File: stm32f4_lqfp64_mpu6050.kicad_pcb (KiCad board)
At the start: 4 copper layers, 130 x 100 mm, 175 parts, among them M5 ALIS-CUSTOM-PARTS_POWERPADS, P1 CONN_01X08, P2 CONN_02X08, Q5 BSS138, Q6 CRYSTAL_50X32, U1 STM32F405R, U2 MPU6050, U3 LP2985LV, U4 LP2985LV, U5 W25Q80BV, U6 LMH1980, U7 TS5A3160, U8 TS5A3160, U9 LT6206, X1 CON-JST_SM04B-SRSS-TB, X2 CON-JST_SM04B-SRSS-TB, X4 CON-JST_SM04B-SRSS-TB

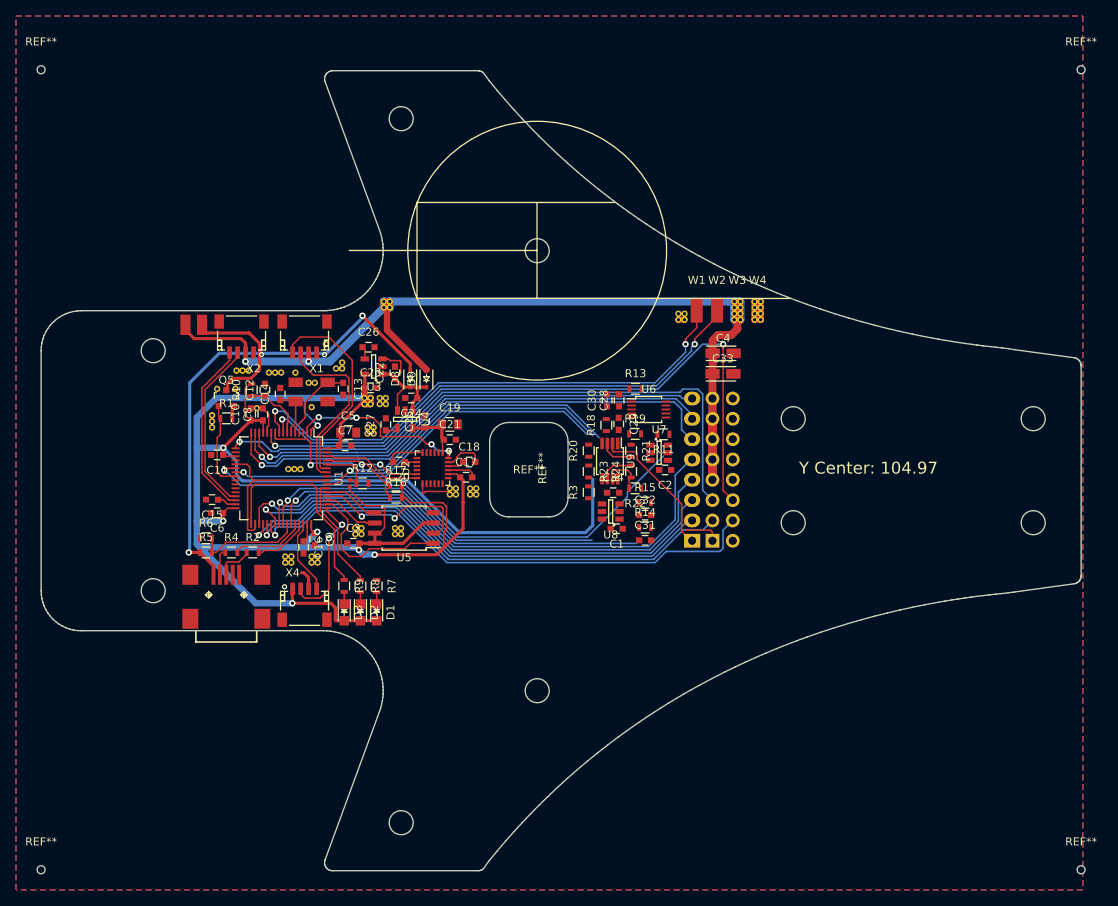
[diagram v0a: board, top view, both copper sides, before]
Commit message: routing finished - essential signals only
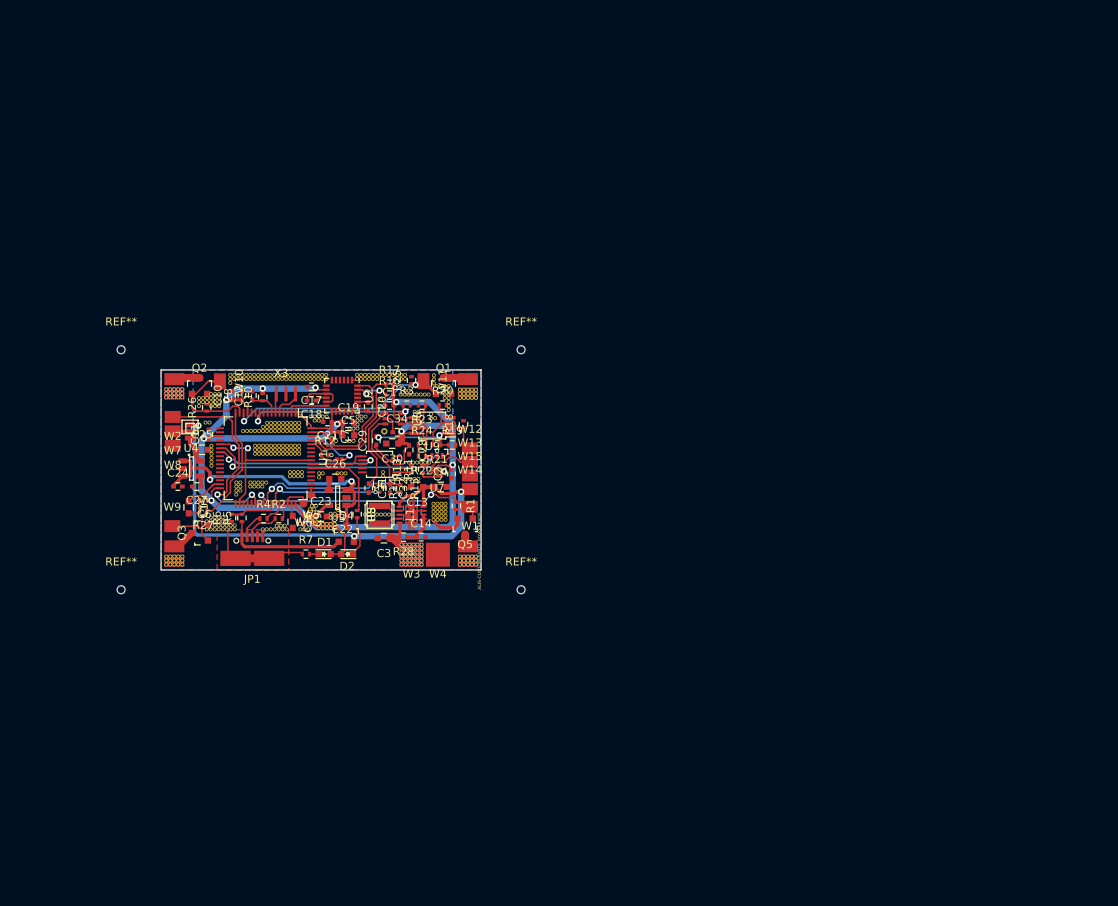
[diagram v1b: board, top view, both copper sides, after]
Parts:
- removed the ? at (173.1, 86.2)
- removed the ? at (172.3, 86.2)
- removed the ? at (126.7, 83.9)
- removed the ? at (126.0, 83.9)
- removed the ? at (126.0, 84.7)
- removed the ? at (126.7, 84.7)
- removed the ? at (170.6, 84.7)
- removed the ? at (170.6, 83.9)
- removed the ? at (169.8, 83.9)
- removed the ? at (169.8, 84.7)
- removed the ? at (170.6, 86.2)
- removed the ? at (120.0, 92.3)
- removed the ? at (170.6, 85.5)
- removed the ? at (169.8, 85.5)
- removed the ? at (169.8, 86.2)
- removed the ? at (124.3, 96.0)
- removed the ? at (124.3, 96.8)
- removed the ? at (123.6, 96.8)
- removed the ? at (104.5, 98.2)
- removed the ? at (104.5, 98.9)
- removed the ? at (104.5, 99.7)
- removed the ? at (123.2, 113.0)
- removed the ? at (172.3, 83.9)
- removed the ? at (122.4, 113.0)
- removed the ? at (122.4, 112.3)
- removed the ? at (123.2, 112.3)
- removed the ? at (117.7, 115.8)
- removed the ? at (117.7, 116.6)
- removed the ? at (117.0, 116.6)
- removed the ? at (117.0, 115.8)
- removed the ? at (127.4, 112.3)
- removed the ? at (128.1, 112.3)
- removed the ? at (128.1, 113.0)
- removed the ? at (117.0, 97.2)
- removed the ? at (127.4, 113.0)
- removed the ? at (123.6, 96.0)
- removed the ? at (136.8, 108.1)
- removed the ? at (137.5, 108.1)
- removed the ? at (137.5, 107.3)
- removed the ? at (136.8, 107.3)
- removed the ? at (134.2, 108.1)
- removed the ? at (134.2, 107.3)
- removed the ? at (135.0, 107.3)
- removed the ? at (135.0, 108.1)
- removed the ? at (173.1, 83.9)
- removed the ? at (124.7, 100.5)
- removed the ? at (125.5, 96.0)
- removed the ? at (126.2, 96.0)
- removed the ? at (126.2, 96.8)
- removed the ? at (125.5, 96.8)
- removed the ? at (124.0, 100.5)
- removed the ? at (124.0, 99.7)
- removed the ? at (124.7, 99.7)
- removed the ? at (162.8, 86.2)
- removed the ? at (163.6, 86.2)
- removed the ? at (173.1, 84.7)
- removed the ? at (162.8, 85.5)
- removed the ? at (163.6, 85.5)
- removed the ? at (110.1, 97.3)
- removed the ? at (115.6, 104.9)
- removed the ? at (114.8, 104.9)
- removed the ? at (114.0, 104.9)
- removed the ? at (114.4, 116.6)
- removed the ? at (113.7, 115.8)
- removed the ? at (113.7, 116.6)
- removed the ? at (114.4, 115.8)
- removed the ? at (172.3, 84.7)
- removed the ? at (120.8, 92.3)
- removed the ? at (120.8, 91.6)
- removed the ? at (118.7, 89.3)
- removed the ? at (117.3, 94.1)
- removed the ? at (116.6, 94.1)
- removed the ? at (114.9, 92.8)
- removed the ? at (113.2, 92.8)
- removed the ? at (112.4, 92.8)
- removed the ? at (111.6, 92.8)
- removed the ? at (109.1, 92.6)
- removed the ? at (173.1, 85.5)
- removed the ? at (108.3, 92.6)
- removed the ? at (107.6, 92.6)
- removed the ? at (105.2, 94.9)
- removed the ? at (107.4, 94.9)
- removed the ? at (172.3, 85.5)
- removed C33: 4u7, Capacitors_Tantalum_SMD:TantalC_SizeA_EIA-3216_Reflow
- removed D3: Red, LEDs:LED-0805
- removed D8, D9: D_Schottky_Small, Diodes_SMD:SOD-323
- removed P1: CONN_01X08, Pin_Headers:Pin_Header_Straight_1x08
- removed P2: CONN_02X08, Pin_Headers:Pin_Header_Straight_2x08
- removed Q6: CRYSTAL_50X32, minimal:CRYSTAL_50X32
- removed R9: 100R, Resistors_SMD:R_0603
- removed the REF** at (145.3, 104.8)
- removed the REF** at (144.1, 105.0)
- removed X1, X2, X4: CON-JST_SM04B-SRSS-TB, Connectors_JST_SH:Connectors_JST_SM04B-SRSS-TB
- added ?: , alis_parts:via_04_no_front_mask, F.Cu at (118.3, 93.6)
- added ?: , alis_parts:via_04_no_front_mask, F.Cu at (107.8, 93.6)
- added ?: , alis_parts:via_04_no_front_mask, F.Cu at (137.0, 116.3)
- added ?: , alis_parts:via_04_no_front_mask, F.Cu at (136.0, 116.3)
- added ?: , alis_parts:via_04_no_front_mask, F.Cu at (136.5, 116.3)
- added ?: , alis_parts:via_04_no_front_mask, F.Cu at (128.7, 114.8)
- added ?: , alis_parts:via_04_no_front_mask, F.Cu at (129.7, 114.8)
- added ?: , alis_parts:via_04_no_front_mask, F.Cu at (130.2, 114.8)
- added ?: , alis_parts:via_04_no_front_mask, F.Cu at (129.2, 114.8)
- added ?: , alis_parts:via_04_no_front_mask, F.Cu at (129.2, 116.3)
- added ?: , alis_parts:via_04_no_front_mask, F.Cu at (128.7, 116.3)
- added ?: , alis_parts:via_04_no_front_mask, F.Cu at (129.7, 116.3)
- added ?: , alis_parts:via_04_no_front_mask, F.Cu at (108.3, 93.6)
- added ?: , alis_parts:via_04_no_front_mask, F.Cu at (130.2, 116.3)
- added ?: , alis_parts:via_04_no_front_mask, F.Cu at (128.7, 115.8)
- added ?: , alis_parts:via_04_no_front_mask, F.Cu at (128.7, 115.3)
- added ?: , alis_parts:via_04_no_front_mask, F.Cu at (130.2, 115.3)
- added ?: , alis_parts:via_04_no_front_mask, F.Cu at (130.2, 115.8)
- added ?: , alis_parts:via_04_no_front_mask, F.Cu at (136.0, 95.5)
- added ?: , alis_parts:via_04_no_front_mask, F.Cu at (136.5, 95.5)
- added ?: , alis_parts:via_04_no_front_mask, F.Cu at (137.0, 95.5)
- added ?: , alis_parts:via_04_no_front_mask, F.Cu at (100.3, 95.4)
- added ?: , alis_parts:via_04_no_front_mask, F.Cu at (99.3, 95.4)
- added ?: , alis_parts:via_04_no_front_mask, F.Cu at (111.8, 93.6)
- added ?: , alis_parts:via_04_no_front_mask, F.Cu at (99.8, 95.4)
- added ?: , alis_parts:via_04_no_front_mask, F.Cu at (129.7, 115.3)
- added ?: , alis_parts:via_04_no_front_mask, F.Cu at (129.7, 114.3)
- added ?: , alis_parts:via_04_no_front_mask, F.Cu at (130.7, 114.8)
- added ?: , alis_parts:via_04_no_front_mask, F.Cu at (130.7, 114.3)
- added ?: , alis_parts:via_04_no_front_mask, F.Cu at (130.7, 115.3)
- added ?: , alis_parts:via_04_no_front_mask, F.Cu at (130.2, 114.3)
- added ?: , alis_parts:via_04_no_front_mask, F.Cu at (128.2, 114.8)
- added ?: , alis_parts:via_04_no_front_mask, F.Cu at (128.2, 115.3)
- added ?: , alis_parts:via_04_no_front_mask, F.Cu at (128.2, 114.3)
- added ?: , alis_parts:via_04_no_front_mask, F.Cu at (112.3, 93.6)
- added ?: , alis_parts:via_04_no_front_mask, F.Cu at (129.2, 114.3)
- added ?: , alis_parts:via_04_no_front_mask, F.Cu at (129.2, 115.3)
- added ?: , alis_parts:via_04_no_front_mask, F.Cu at (128.7, 114.3)
- added ?: , alis_parts:via_04_no_front_mask, F.Cu at (128.2, 116.3)
- added ?: , alis_parts:via_04_no_front_mask, F.Cu at (128.2, 116.8)
- added ?: , alis_parts:via_04_no_front_mask, F.Cu at (128.2, 115.8)
- added ?: , alis_parts:via_04_no_front_mask, F.Cu at (129.2, 115.8)
- added ?: , alis_parts:via_04_no_front_mask, F.Cu at (129.2, 116.8)
- added ?: , alis_parts:via_04_no_front_mask, F.Cu at (128.7, 116.8)
- added ?: , alis_parts:via_04_no_front_mask, F.Cu at (129.7, 116.8)
- added ?: , alis_parts:via_04_no_front_mask, F.Cu at (112.8, 93.6)
- added ?: , alis_parts:via_04_no_front_mask, F.Cu at (129.7, 115.8)
- added ?: , alis_parts:via_04_no_front_mask, F.Cu at (130.7, 116.3)
- added ?: , alis_parts:via_04_no_front_mask, F.Cu at (130.7, 115.8)
- added ?: , alis_parts:via_04_no_front_mask, F.Cu at (130.7, 116.8)
- added ?: , alis_parts:via_04_no_front_mask, F.Cu at (130.2, 116.8)
- added ?: , alis_parts:via_04_no_front_mask, F.Cu at (133.2, 109.2)
- added ?: , alis_parts:via_04_no_front_mask, F.Cu at (133.7, 109.2)
- added ?: , alis_parts:via_04_no_front_mask, F.Cu at (132.7, 109.2)
- added ?: , alis_parts:via_04_no_front_mask, F.Cu at (132.2, 109.2)
- added ?: , alis_parts:via_04_no_front_mask, F.Cu at (133.7, 110.2)
- added ?: , alis_parts:via_04_no_front_mask, F.Cu at (113.3, 93.6)
- added ?: , alis_parts:via_04_no_front_mask, F.Cu at (133.7, 111.2)
- added ?: , alis_parts:via_04_no_front_mask, F.Cu at (133.7, 109.7)
- added ?: , alis_parts:via_04_no_front_mask, F.Cu at (133.7, 110.7)
- added ?: , alis_parts:via_04_no_front_mask, F.Cu at (133.2, 109.7)
- added ?: , alis_parts:via_04_no_front_mask, F.Cu at (133.2, 110.7)
- added ?: , alis_parts:via_04_no_front_mask, F.Cu at (133.2, 110.2)
- added ?: , alis_parts:via_04_no_front_mask, F.Cu at (133.2, 111.2)
- added ?: , alis_parts:via_04_no_front_mask, F.Cu at (103.0, 109.2)
- added ?: , alis_parts:via_04_no_front_mask, F.Cu at (103.0, 109.7)
- added ?: , alis_parts:via_04_no_front_mask, F.Cu at (125.6, 96.2)
- added ?: , alis_parts:via_04_no_front_mask, F.Cu at (114.3, 93.6)
- added ?: , alis_parts:via_04_no_front_mask, F.Cu at (108.0, 107.6)
- added ?: , alis_parts:via_04_no_front_mask, F.Cu at (108.0, 107.1)
- added ?: , alis_parts:via_04_no_front_mask, F.Cu at (107.5, 108.1)
- added ?: , alis_parts:via_04_no_front_mask, F.Cu at (107.5, 107.6)
- added ?: , alis_parts:via_04_no_front_mask, F.Cu at (107.5, 107.1)
- added ?: , alis_parts:via_04_no_front_mask, F.Cu at (107.5, 106.6)
- added ?: , alis_parts:via_04_no_front_mask, F.Cu at (108.0, 106.6)
- added ?: , alis_parts:via_04_no_front_mask, F.Cu at (122.2, 101.4)
- added ?: , alis_parts:via_04_no_front_mask, F.Cu at (121.7, 101.4)
- added ?: , alis_parts:via_04_no_front_mask, F.Cu at (120.0, 101.4)
- added ?: , alis_parts:via_04_no_front_mask, F.Cu at (114.8, 93.6)
- added ?: , alis_parts:via_04_no_front_mask, F.Cu at (104.2, 99.1)
- added ?: , alis_parts:via_04_no_front_mask, F.Cu at (103.7, 99.1)
- added ?: , alis_parts:via_04_no_front_mask, F.Cu at (104.4, 104.5)
- added ?: , alis_parts:via_04_no_front_mask, F.Cu at (104.4, 104.0)
- added ?: , alis_parts:via_04_no_front_mask, F.Cu at (104.4, 103.5)
- added ?: , alis_parts:via_04_no_front_mask, F.Cu at (104.4, 103.0)
- added ?: , alis_parts:via_04_no_front_mask, F.Cu at (104.4, 102.5)
- added ?: , alis_parts:via_04_no_front_mask, F.Cu at (104.4, 102.0)
- added ?: , alis_parts:via_04_no_front_mask, F.Cu at (131.6, 104.1)
- added ?: , alis_parts:via_04_no_front_mask, F.Cu at (131.1, 104.1)
- added ?: , alis_parts:via_04_no_front_mask, F.Cu at (115.3, 93.6)
- added ?: , alis_parts:via_04_no_front_mask, F.Cu at (130.6, 104.1)
- added ?: , alis_parts:via_04_no_front_mask, F.Cu at (130.1, 104.1)
- added ?: , alis_parts:via_04_no_front_mask, F.Cu at (129.6, 104.1)
- added ?: , alis_parts:via_04_no_front_mask, F.Cu at (127.8, 106.1)
- added ?: , alis_parts:via_04_no_front_mask, F.Cu at (128.3, 106.1)
- added ?: , alis_parts:via_04_no_front_mask, F.Cu at (128.8, 106.1)
- added ?: , alis_parts:via_04_no_front_mask, F.Cu at (129.3, 106.1)
- added ?: , alis_parts:via_04_no_front_mask, F.Cu at (129.8, 106.1)
- added ?: , alis_parts:via_04_no_front_mask, F.Cu at (130.3, 106.1)
- added ?: , alis_parts:via_04_no_front_mask, F.Cu at (110.8, 107.1)
- added ?: , alis_parts:via_04_no_front_mask, F.Cu at (113.8, 93.6)
- added ?: , alis_parts:via_04_no_front_mask, F.Cu at (110.3, 107.1)
- added ?: , alis_parts:via_04_no_front_mask, F.Cu at (109.8, 107.1)
- added ?: , alis_parts:via_04_no_front_mask, F.Cu at (109.3, 107.1)
- added ?: , alis_parts:via_04_no_front_mask, F.Cu at (111.3, 106.6)
- added ?: , alis_parts:via_04_no_front_mask, F.Cu at (110.8, 106.6)
- added ?: , alis_parts:via_04_no_front_mask, F.Cu at (110.3, 106.6)
- added ?: , alis_parts:via_04_no_front_mask, F.Cu at (109.8, 106.6)
- added ?: , alis_parts:via_04_no_front_mask, F.Cu at (109.3, 106.6)
- added ?: , alis_parts:via_04_no_front_mask, F.Cu at (115.7, 105.8)
- added ?: , alis_parts:via_04_no_front_mask, F.Cu at (115.2, 105.8)
- added ?: , alis_parts:via_04_no_front_mask, F.Cu at (118.8, 93.6)
- added ?: , alis_parts:via_04_no_front_mask, F.Cu at (115.8, 93.6)
- added ?: , alis_parts:via_04_no_front_mask, F.Cu at (114.7, 105.8)
- added ?: , alis_parts:via_04_no_front_mask, F.Cu at (114.2, 105.8)
- added ?: , alis_parts:via_04_no_front_mask, F.Cu at (114.2, 105.3)
- added ?: , alis_parts:via_04_no_front_mask, F.Cu at (114.7, 105.3)
- added ?: , alis_parts:via_04_no_front_mask, F.Cu at (115.2, 105.3)
- added ?: , alis_parts:via_04_no_front_mask, F.Cu at (115.7, 105.3)
- added ?: , alis_parts:via_04_no_front_mask, F.Cu at (109.9, 102.0)
- added ?: , alis_parts:via_04_no_front_mask, F.Cu at (110.4, 102.0)
- added ?: , alis_parts:via_04_no_front_mask, F.Cu at (110.9, 102.0)
- added ?: , alis_parts:via_04_no_front_mask, F.Cu at (111.4, 102.0)
- added ?: , alis_parts:via_04_no_front_mask, F.Cu at (116.3, 93.6)
- added ?: , alis_parts:via_04_no_front_mask, F.Cu at (111.9, 102.0)
- added ?: , alis_parts:via_04_no_front_mask, F.Cu at (112.4, 102.0)
- added ?: , alis_parts:via_04_no_front_mask, F.Cu at (112.9, 102.0)
- added ?: , alis_parts:via_04_no_front_mask, F.Cu at (113.4, 102.0)
- added ?: , alis_parts:via_04_no_front_mask, F.Cu at (113.9, 102.0)
- added ?: , alis_parts:via_04_no_front_mask, F.Cu at (114.4, 102.0)
- added ?: , alis_parts:via_04_no_front_mask, F.Cu at (114.9, 102.0)
- added ?: , alis_parts:via_04_no_front_mask, F.Cu at (115.4, 102.0)
- added ?: , alis_parts:via_04_no_front_mask, F.Cu at (108.4, 100.1)
- added ?: , alis_parts:via_04_no_front_mask, F.Cu at (108.9, 100.1)
- added ?: , alis_parts:via_04_no_front_mask, F.Cu at (116.8, 93.6)
- added ?: , alis_parts:via_04_no_front_mask, F.Cu at (109.4, 100.1)
- added ?: , alis_parts:via_04_no_front_mask, F.Cu at (109.9, 100.1)
- added ?: , alis_parts:via_04_no_front_mask, F.Cu at (110.4, 100.1)
- added ?: , alis_parts:via_04_no_front_mask, F.Cu at (110.9, 100.1)
- added ?: , alis_parts:via_04_no_front_mask, F.Cu at (111.4, 100.1)
- added ?: , alis_parts:via_04_no_front_mask, F.Cu at (111.9, 100.1)
- added ?: , alis_parts:via_04_no_front_mask, F.Cu at (112.4, 100.1)
- added ?: , alis_parts:via_04_no_front_mask, F.Cu at (112.9, 100.1)
- added ?: , alis_parts:via_04_no_front_mask, F.Cu at (113.4, 100.1)
- added ?: , alis_parts:via_04_no_front_mask, F.Cu at (113.9, 100.1)
- added ?: , alis_parts:via_04_no_front_mask, F.Cu at (117.3, 93.6)
- added ?: , alis_parts:via_04_no_front_mask, F.Cu at (114.4, 100.1)
- added ?: , alis_parts:via_04_no_front_mask, F.Cu at (114.9, 100.1)
- added ?: , alis_parts:via_04_no_front_mask, F.Cu at (115.4, 100.1)
- added ?: , alis_parts:via_04_no_front_mask, F.Cu at (117.8, 98.8)
- added ?: , alis_parts:via_04_no_front_mask, F.Cu at (117.3, 98.8)
- added ?: , alis_parts:via_04_no_front_mask, F.Cu at (116.8, 98.3)
- added ?: , alis_parts:via_04_no_front_mask, F.Cu at (117.3, 98.3)
- added ?: , alis_parts:via_04_no_front_mask, F.Cu at (117.8, 98.3)
- added ?: , alis_parts:via_04_no_front_mask, F.Cu at (118.3, 98.3)
- added ?: , alis_parts:via_04_no_front_mask, F.Cu at (118.8, 98.3)
- added ?: , alis_parts:via_04_no_front_mask, F.Cu at (117.8, 93.6)
- added ?: , alis_parts:via_04_no_front_mask, F.Cu at (121.7, 99.8)
- added ?: , alis_parts:via_04_no_front_mask, F.Cu at (122.2, 99.8)
- added ?: , alis_parts:via_04_no_front_mask, F.Cu at (122.7, 99.8)
- added ?: , alis_parts:via_04_no_front_mask, F.Cu at (122.7, 99.3)
- added ?: , alis_parts:via_04_no_front_mask, F.Cu at (122.7, 98.8)
- added ?: , alis_parts:via_04_no_front_mask, F.Cu at (122.7, 98.3)
- added ?: , alis_parts:via_04_no_front_mask, F.Cu at (123.2, 98.8)
- added ?: , alis_parts:via_04_no_front_mask, F.Cu at (123.2, 98.3)
- added ?: , alis_parts:via_04_no_front_mask, F.Cu at (123.7, 98.3)
- added ?: , alis_parts:via_04_no_front_mask, F.Cu at (129.8, 97.7)
- added ?: , alis_parts:via_04_no_front_mask, F.Cu at (128.1, 93.6)
- added ?: , alis_parts:via_04_no_front_mask, F.Cu at (130.3, 97.7)
- added ?: , alis_parts:via_04_no_front_mask, F.Cu at (131.9, 98.0)
- added ?: , alis_parts:via_04_no_front_mask, F.Cu at (131.9, 98.5)
- added ?: , alis_parts:via_04_no_front_mask, F.Cu at (132.4, 98.5)
- added ?: , alis_parts:via_04_no_front_mask, F.Cu at (129.1, 104.1)
- added ?: , alis_parts:via_04_no_front_mask, F.Cu at (125.9, 105.8)
- added ?: , alis_parts:via_04_no_front_mask, F.Cu at (125.9, 105.3)
- added ?: , alis_parts:via_04_no_front_mask, F.Cu at (132.2, 109.7)
- added ?: , alis_parts:via_04_no_front_mask, F.Cu at (132.7, 109.7)
- added ?: , alis_parts:via_04_no_front_mask, F.Cu at (132.7, 110.2)
- added ?: , alis_parts:via_04_no_front_mask, F.Cu at (128.6, 93.6)
- added ?: , alis_parts:via_04_no_front_mask, F.Cu at (132.2, 110.2)
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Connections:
- net BUZZER renamed M4
- net Net-(C29-Pad2) renamed video_buffered
- net Net-(C31-Pad1) renamed W_Filtered
- net Net-(C32-Pad1) renamed B_Filtered
- net Net-(JP2-Pad2) renamed BOOT0
- net Net-(R22-Pad2) renamed bw_buffered
- C13 pad 1: Net-(C13-Pad1) -> 5V
- C19 pad 1: 3.3V_SEN -> 3.3V
- C21 pad 1: 3.3V_SEN -> 3.3V
- C25 pad 1: 3.3V_SEN -> 3.3V_EXT
- C28 pad 1: Net-(C28-Pad1) -> 3.3V
- C3 pad 1: GND -> VBAT
- C3 pad 2: 3.3V -> GND
- C30 pad 1: Net-(C30-Pad1) -> 3.3V
- C4 pad 1: VBAT -> 5V
- Q5 pad 1: MCU_BUZZER -> TIM8_CH4
- R1 pad 1: MCU_BUZZER -> TIM8_CH4
- U1 pad 5: Net-(C13-Pad1) -> Net-(U1-Pad5)
- U1 pad 6: Net-(C14-Pad1) -> Net-(U1-Pad6)
- U2 pad 13: 3.3V_SEN -> 3.3V
- U4 pad 5: 3.3V_SEN -> 3.3V_EXT
- U5 pad 1: FLASH_CS -> 5V
- U5 pad 2: MISO -> Net-(L1-Pad1)
- U5 pad 3: 3.3V -> GND
- U5 pad 4: GND -> Net-(L1-Pad2)
- U5 pad 5: MOSI -> VBAT
- U5 pad 6: SCK -> Net-(C14-Pad1)
- U5 pad 7: 3.3V -> Net-(C14-Pad1)
- U5 pad 8: 3.3V -> Net-(C14-Pad1)
- U6 pad 3: Net-(C30-Pad1) -> 3.3V
- W1 pad 1: ADC2 -> TIM8_CH4
- W2 pad 1: ADC1 -> TIM8_CH2/FRSKY_RSSI/DSM
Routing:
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- added copper zone on B.Cu, net VBAT
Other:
- board size 130 x 100 mm -> 40 x 25 mm
- board text removed: "Alexander Tuxen 2016"
- board text removed: "Flexi Main"
- board text removed: "PPM Servo Back Left Right"
- board text removed: "Vin Vout GND PWM7 PWM8 DSM PWM5 PWM6 ADC3"
- board text removed: "Y Center: 104.97"

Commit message: minor changes
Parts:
- removed the ? at (118.3, 93.6)
- removed the ? at (107.8, 93.6)
- removed the ? at (137.0, 116.3)
- removed the ? at (136.0, 116.3)
- removed the ? at (136.5, 116.3)
- removed the ? at (128.7, 114.8)
- removed the ? at (129.7, 114.8)
- removed the ? at (130.2, 114.8)
- removed the ? at (129.2, 114.8)
- removed the ? at (129.2, 116.3)
- removed the ? at (128.7, 116.3)
- removed the ? at (129.7, 116.3)
- removed the ? at (108.3, 93.6)
- removed the ? at (130.2, 116.3)
- removed the ? at (128.7, 115.8)
- removed the ? at (128.7, 115.3)
- removed the ? at (130.2, 115.3)
- removed the ? at (130.2, 115.8)
- removed the ? at (136.0, 95.5)
- removed the ? at (136.5, 95.5)
- removed the ? at (137.0, 95.5)
- removed the ? at (100.3, 95.4)
- removed the ? at (99.3, 95.4)
- removed the ? at (111.8, 93.6)
- removed the ? at (99.8, 95.4)
- removed the ? at (129.7, 115.3)
- removed the ? at (129.7, 114.3)
- removed the ? at (130.7, 114.8)
- removed the ? at (130.7, 114.3)
- removed the ? at (130.7, 115.3)
- removed the ? at (130.2, 114.3)
- removed the ? at (128.2, 114.8)
- removed the ? at (128.2, 115.3)
- removed the ? at (128.2, 114.3)
- removed the ? at (112.3, 93.6)
- removed the ? at (129.2, 114.3)
- removed the ? at (129.2, 115.3)
- removed the ? at (128.7, 114.3)
- removed the ? at (128.2, 116.3)
- removed the ? at (128.2, 116.8)
- removed the ? at (128.2, 115.8)
- removed the ? at (129.2, 115.8)
- removed the ? at (129.2, 116.8)
- removed the ? at (128.7, 116.8)
- removed the ? at (129.7, 116.8)
- removed the ? at (112.8, 93.6)
- removed the ? at (129.7, 115.8)
- removed the ? at (130.7, 116.3)
- removed the ? at (130.7, 115.8)
- removed the ? at (130.7, 116.8)
- removed the ? at (130.2, 116.8)
- removed the ? at (133.2, 109.2)
- removed the ? at (133.7, 109.2)
- removed the ? at (132.7, 109.2)
- removed the ? at (132.2, 109.2)
- removed the ? at (133.7, 110.2)
- removed the ? at (113.3, 93.6)
- removed the ? at (133.7, 111.2)
- removed the ? at (133.7, 109.7)
- removed the ? at (133.7, 110.7)
- removed the ? at (133.2, 109.7)
- removed the ? at (133.2, 110.7)
- removed the ? at (133.2, 110.2)
- removed the ? at (133.2, 111.2)
- removed the ? at (103.0, 109.2)
- removed the ? at (103.0, 109.7)
- removed the ? at (125.6, 96.2)
- removed the ? at (114.3, 93.6)
- removed the ? at (108.0, 107.6)
- removed the ? at (108.0, 107.1)
- removed the ? at (107.5, 108.1)
- removed the ? at (107.5, 107.6)
- removed the ? at (107.5, 106.6)
- removed the ? at (108.0, 106.6)
- removed the ? at (122.2, 101.4)
- removed the ? at (121.7, 101.4)
- removed the ? at (120.0, 101.4)
- removed the ? at (114.8, 93.6)
- removed the ? at (104.2, 99.1)
- removed the ? at (103.7, 99.1)
- removed the ? at (104.4, 104.5)
- removed the ? at (104.4, 104.0)
- removed the ? at (104.4, 103.5)
- removed the ? at (104.4, 103.0)
- removed the ? at (104.4, 102.5)
- removed the ? at (104.4, 102.0)
- removed the ? at (131.6, 104.1)
- removed the ? at (131.1, 104.1)
- removed the ? at (115.3, 93.6)
- removed the ? at (130.6, 104.1)
- removed the ? at (130.1, 104.1)
- removed the ? at (129.6, 104.1)
- removed the ? at (127.8, 106.1)
- removed the ? at (128.3, 106.1)
- removed the ? at (128.8, 106.1)
- removed the ? at (129.3, 106.1)
- removed the ? at (129.8, 106.1)
- removed the ? at (130.3, 106.1)
- removed the ? at (110.8, 107.1)
- removed the ? at (113.8, 93.6)
- removed the ? at (110.3, 107.1)
- removed the ? at (109.8, 107.1)
- removed the ? at (109.3, 107.1)
- removed the ? at (111.3, 106.6)
- removed the ? at (110.8, 106.6)
- removed the ? at (110.3, 106.6)
- removed the ? at (109.8, 106.6)
- removed the ? at (109.3, 106.6)
- removed the ? at (115.7, 105.8)
- removed the ? at (115.2, 105.8)
- removed the ? at (118.8, 93.6)
- removed the ? at (115.8, 93.6)
- removed the ? at (114.7, 105.8)
- removed the ? at (114.2, 105.8)
- removed the ? at (114.2, 105.3)
- removed the ? at (114.7, 105.3)
- removed the ? at (115.2, 105.3)
- removed the ? at (115.7, 105.3)
- removed the ? at (109.9, 102.0)
- removed the ? at (110.4, 102.0)
- removed the ? at (110.9, 102.0)
- removed the ? at (111.4, 102.0)
- removed the ? at (116.3, 93.6)
- removed the ? at (111.9, 102.0)
- removed the ? at (112.4, 102.0)
- removed the ? at (112.9, 102.0)
- removed the ? at (113.4, 102.0)
- removed the ? at (113.9, 102.0)
- removed the ? at (114.4, 102.0)
- removed the ? at (114.9, 102.0)
- removed the ? at (115.4, 102.0)
- removed the ? at (108.4, 100.1)
- removed the ? at (108.9, 100.1)
- removed the ? at (116.8, 93.6)
- removed the ? at (109.4, 100.1)
- removed the ? at (109.9, 100.1)
- removed the ? at (110.4, 100.1)
- removed the ? at (110.9, 100.1)
- removed the ? at (111.4, 100.1)
- removed the ? at (111.9, 100.1)
- removed the ? at (112.4, 100.1)
- removed the ? at (112.9, 100.1)
- removed the ? at (113.4, 100.1)
- removed the ? at (113.9, 100.1)
- removed the ? at (117.3, 93.6)
- removed the ? at (114.4, 100.1)
- removed the ? at (114.9, 100.1)
- removed the ? at (115.4, 100.1)
- removed the ? at (117.8, 98.8)
- removed the ? at (117.3, 98.8)
- removed the ? at (116.8, 98.3)
- removed the ? at (117.3, 98.3)
- removed the ? at (117.8, 98.3)
- removed the ? at (118.3, 98.3)
- removed the ? at (118.8, 98.3)
- removed the ? at (117.8, 93.6)
- removed the ? at (121.7, 99.8)
- removed the ? at (122.2, 99.8)
- removed the ? at (122.7, 99.8)
- removed the ? at (122.7, 99.3)
- removed the ? at (122.7, 98.8)
- removed the ? at (122.7, 98.3)
- removed the ? at (123.2, 98.8)
- removed the ? at (123.7, 98.3)
- removed the ? at (129.8, 97.7)
- removed the ? at (128.1, 93.6)
- removed the ? at (130.3, 97.7)
- removed the ? at (131.9, 98.0)
- removed the ? at (131.9, 98.5)
- removed the ? at (132.4, 98.5)
- removed the ? at (129.1, 104.1)
- removed the ? at (125.9, 105.8)
- removed the ? at (125.9, 105.3)
- removed the ? at (132.2, 109.7)
- removed the ? at (132.7, 109.7)
- removed the ? at (132.7, 110.2)
- removed the ? at (128.6, 93.6)
- removed the ? at (132.2, 110.2)
- removed the ? at (132.2, 110.7)
- removed the ? at (132.7, 110.7)
- removed the ? at (132.2, 111.2)
- removed the ? at (132.7, 111.2)
- removed the ? at (99.8, 94.9)
- removed the ? at (100.3, 94.9)
- removed the ? at (100.8, 94.9)
- removed the ? at (99.8, 95.9)
- removed the ? at (100.3, 95.9)
- removed the ? at (124.6, 93.6)
- removed the ? at (100.8, 95.9)
- removed the ? at (100.8, 95.4)
- removed the ? at (98.8, 95.9)
- removed the ? at (98.8, 95.4)
- removed the ? at (98.8, 94.9)
- removed the ? at (99.3, 94.9)
- removed the ? at (99.3, 95.9)
- removed the ? at (99.8, 115.8)
- removed the ? at (100.3, 115.8)
- removed the ? at (100.8, 115.8)
- removed the ? at (124.1, 93.6)
- removed the ? at (99.8, 116.8)
- removed the ? at (100.3, 116.8)
- removed the ? at (100.8, 116.8)
- removed the ? at (100.8, 116.3)
- removed the ? at (98.8, 116.8)
- removed the ? at (98.8, 116.3)
- removed the ? at (98.8, 115.8)
- removed the ? at (99.3, 115.8)
- removed the ? at (99.3, 116.8)
- removed the ? at (136.5, 115.8)
- removed the ? at (123.6, 93.6)
- removed the ? at (137.0, 115.8)
- removed the ? at (137.5, 115.8)
- removed the ? at (136.5, 116.8)
- removed the ? at (137.0, 116.8)
- removed the ? at (137.5, 116.8)
- removed the ? at (137.5, 116.3)
- removed the ? at (135.5, 116.8)
- removed the ? at (135.5, 116.3)
- removed the ? at (135.5, 115.8)
- removed the ? at (136.0, 115.8)
- removed the ? at (109.8, 93.6)
- removed the ? at (125.1, 93.6)
- removed the ? at (136.0, 116.8)
- removed the ? at (135.5, 96.0)
- removed the ? at (135.5, 95.5)
- removed the ? at (135.5, 95.0)
- removed the ? at (136.0, 95.0)
- removed the ? at (136.0, 96.0)
- removed the ? at (136.5, 96.0)
- removed the ? at (136.5, 95.0)
- removed the ? at (137.0, 95.0)
- removed the ? at (137.0, 96.0)
- removed the ? at (123.1, 93.6)
- removed the ? at (137.5, 96.0)
- removed the ? at (137.5, 95.5)
- removed the ? at (137.5, 95.0)
- removed the ? at (118.8, 93.1)
- removed the ? at (118.3, 93.1)
- removed the ? at (117.8, 93.1)
- removed the ? at (117.3, 93.1)
- removed the ? at (116.8, 93.1)
- removed the ? at (116.3, 93.1)
- removed the ? at (115.8, 93.1)
- removed the ? at (122.6, 93.6)
- removed the ? at (115.3, 93.1)
- removed the ? at (114.8, 93.1)
- removed the ? at (114.3, 93.1)
- removed the ? at (113.8, 93.1)
- removed the ? at (113.3, 93.1)
- removed the ? at (112.8, 93.1)
- removed the ? at (112.3, 93.1)
- removed the ? at (111.8, 93.1)
- removed the ? at (111.3, 93.1)
- removed the ? at (110.8, 93.1)
- removed the ? at (120.2, 109.5)
- removed the ? at (110.3, 93.1)
- removed the ? at (109.8, 93.1)
- removed the ? at (122.6, 93.1)
- removed the ? at (123.1, 93.1)
- removed the ? at (123.6, 93.1)
- removed the ? at (124.1, 93.1)
- removed the ? at (124.6, 93.1)
- removed the ? at (125.1, 93.1)
- removed the ? at (125.6, 93.1)
- removed the ? at (126.1, 93.1)
- removed the ? at (120.2, 110.0)
- removed the ? at (126.6, 93.1)
- removed the ? at (127.1, 93.1)
- removed the ? at (127.6, 93.1)
- removed the ? at (128.1, 93.1)
- removed the ? at (128.6, 93.1)
- removed the ? at (129.1, 95.1)
- removed the ? at (128.6, 95.1)
- removed the ? at (128.1, 95.6)
- removed the ? at (128.6, 95.6)
- removed the ? at (129.1, 95.6)
- removed the ? at (119.3, 110.5)
- removed the ? at (129.6, 95.6)
- removed the ? at (130.1, 95.6)
- removed the ? at (130.6, 95.6)
- removed the ? at (131.1, 95.6)
- removed the ? at (131.6, 95.6)
- removed the ? at (134.1, 97.5)
- removed the ? at (134.1, 97.0)
- removed the ? at (134.1, 96.5)
- removed the ? at (132.2, 93.2)
- removed the ? at (132.2, 93.7)
- removed the ? at (119.8, 110.5)
- removed the ? at (132.2, 94.2)
- removed the ? at (132.6, 94.5)
- removed the ? at (133.1, 94.5)
- removed the ? at (133.6, 94.5)
- removed the ? at (133.6, 95.0)
- removed the ? at (133.6, 95.5)
- removed the ? at (133.6, 96.0)
- removed the ? at (134.1, 96.0)
- removed the ? at (134.1, 95.5)
- removed the ? at (134.1, 95.0)
- removed the ? at (119.8, 111.0)
- removed the ? at (134.1, 94.5)
- removed the ? at (109.3, 93.1)
- removed the ? at (108.8, 93.1)
- removed the ? at (108.3, 93.1)
- removed the ? at (107.8, 93.1)
- removed the ? at (107.3, 93.1)
- removed the ? at (106.8, 94.1)
- removed the ? at (106.8, 93.6)
- removed the ? at (106.8, 93.1)
- removed the ? at (102.9, 97.0)
- removed the ? at (119.3, 111.0)
- removed the ? at (102.9, 96.5)
- removed the ? at (102.9, 96.0)
- removed the ? at (103.4, 96.0)
- removed the ? at (103.4, 96.5)
- removed the ? at (103.9, 96.5)
- removed the ? at (103.9, 96.0)
- removed the ? at (104.4, 96.0)
- removed the ? at (104.4, 95.5)
- removed the ? at (104.9, 96.0)
- removed the ? at (104.9, 95.5)
- removed the ? at (116.3, 110.8)
- removed the ? at (105.4, 96.0)
- removed the ? at (105.4, 96.5)
- removed the ? at (104.9, 96.5)
- removed the ? at (104.4, 96.5)
- removed the ? at (104.4, 97.0)
- removed the ? at (104.9, 97.0)
- removed the ? at (105.4, 97.0)
- removed the ? at (105.8, 110.9)
- removed the ? at (105.3, 110.9)
- removed the ? at (110.3, 93.6)
- removed the ? at (116.8, 110.8)
- removed the ? at (104.8, 110.9)
- removed the ? at (104.3, 110.9)
- removed the ? at (106.3, 111.4)
- removed the ? at (105.8, 111.4)
- removed the ? at (105.3, 111.4)
- removed the ? at (104.8, 111.4)
- removed the ? at (104.3, 111.4)
- removed the ? at (103.8, 111.4)
- removed the ? at (104.8, 111.9)
- removed the ? at (105.3, 111.9)
- removed the ? at (116.8, 111.3)
- removed the ? at (105.8, 111.9)
- removed the ? at (106.3, 111.9)
- removed the ? at (106.8, 111.9)
- removed the ? at (107.3, 111.9)
- removed the ? at (107.3, 112.4)
- removed the ? at (106.8, 112.4)
- removed the ? at (106.3, 112.4)
- removed the ? at (105.8, 112.4)
- removed the ? at (105.3, 112.4)
- removed the ? at (104.8, 112.4)
- removed the ? at (117.3, 111.3)
- removed the ? at (104.3, 112.4)
- removed the ? at (103.8, 112.4)
- removed the ? at (113.6, 112.0)
- removed the ? at (113.1, 112.0)
- removed the ? at (112.6, 112.0)
- removed the ? at (110.8, 112.4)
- removed the ? at (111.3, 112.4)
- removed the ? at (111.8, 112.4)
- removed the ? at (112.3, 112.4)
- removed the ? at (112.8, 112.4)
- removed the ? at (117.3, 111.8)
- removed the ? at (113.3, 112.4)
- removed the ? at (113.8, 112.4)
- removed the ? at (115.5, 111.7)
- removed the ? at (115.5, 112.4)
- removed the ? at (116.0, 112.4)
- removed the ? at (116.5, 112.4)
- removed the ? at (123.6, 110.6)
- removed the ? at (124.1, 110.6)
- removed the ? at (124.6, 110.6)
- removed the ? at (125.1, 110.6)
- removed the ? at (119.8, 111.8)
- removed the ? at (125.6, 110.6)
- removed the ? at (126.1, 110.6)
- removed the ? at (126.6, 110.6)
- removed the ? at (117.5, 109.5)
- removed the ? at (117.0, 109.5)
- removed the ? at (116.7, 109.9)
- removed the ? at (117.2, 109.9)
- removed the ? at (117.9, 105.9)
- removed the ? at (118.3, 105.4)
- removed the ? at (117.9, 105.4)
- removed the ? at (119.3, 111.8)
- removed the ? at (120.2, 105.4)
- removed the ? at (120.7, 105.4)
- removed the ? at (121.2, 105.4)
- removed the ? at (126.0, 100.2)
- removed the ? at (118.8, 111.8)
- removed the ? at (118.3, 111.8)
- removed the ? at (117.8, 111.8)
- removed the ? at (117.8, 112.3)
- removed the ? at (109.3, 93.6)
- removed the ? at (118.3, 112.3)
- removed the ? at (118.8, 112.3)
- removed the ? at (119.3, 112.3)
- removed the ? at (119.8, 112.3)
- removed the ? at (111.9, 99.1)
- removed the ? at (111.4, 99.1)
- removed the ? at (112.4, 99.1)
- removed the ? at (112.9, 99.1)
- removed the ? at (113.9, 99.1)
- removed the ? at (115.4, 99.1)
- removed the ? at (110.8, 93.6)
- removed the ? at (114.9, 99.1)
- removed the ? at (114.4, 99.1)
- removed the ? at (113.4, 99.1)
- removed the ? at (110.9, 99.6)
- removed the ? at (112.4, 99.6)
- removed the ? at (111.9, 99.6)
- removed the ? at (112.9, 99.6)
- removed the ? at (111.4, 99.6)
- removed the ? at (113.4, 99.6)
- removed the ? at (114.4, 99.6)
- removed the ? at (111.3, 93.6)
- removed the ? at (115.4, 99.6)
- removed the ? at (114.9, 99.6)
- removed the ? at (113.9, 99.6)
- removed the ? at (109.9, 103.0)
- removed the ? at (110.4, 103.0)
- removed the ? at (110.9, 103.0)
- removed the ? at (112.4, 103.0)
- removed the ? at (111.9, 103.0)
- removed the ? at (112.9, 103.0)
- removed the ? at (111.4, 103.0)
- removed the ? at (108.8, 93.6)
- removed the ? at (113.4, 103.0)
- removed the ? at (114.4, 103.0)
- removed the ? at (115.4, 103.0)
- removed the ? at (114.9, 103.0)
- removed the ? at (113.9, 103.0)
- removed the ? at (109.9, 102.5)
- removed the ? at (110.4, 102.5)
- removed the ? at (110.9, 102.5)
- removed the ? at (112.4, 102.5)
- removed the ? at (111.9, 102.5)
- removed the ? at (107.3, 93.6)
- removed the ? at (112.9, 102.5)
- removed the ? at (111.4, 102.5)
- removed the ? at (113.4, 102.5)
- removed the ? at (114.4, 102.5)
- removed the ? at (115.4, 102.5)
- removed the ? at (114.9, 102.5)
- removed the ? at (113.9, 102.5)
- removed the ? at (99.8, 116.3)
- removed the ? at (100.3, 116.3)
- removed the ? at (99.3, 116.3)
- removed REF** (x4): PositioningHole_1mm, alis_parts:PositioningHole_1mm
- added ?: , alis_parts:via_04_no_front_mask, F.Cu at (117.6, 99.1)
- added ?: , alis_parts:via_04_no_front_mask, F.Cu at (112.5, 113.0)
- added ?: , alis_parts:via_04_no_front_mask, F.Cu at (127.1, 99.1)
- added ?: , alis_parts:via_04_no_front_mask, F.Cu at (126.2, 100.3)
- added ?: , alis_parts:via_04_no_front_mask, F.Cu at (126.4, 102.6)
- added ?: , alis_parts:via_04_no_front_mask, F.Cu at (127.1, 102.6)
- added ?: , alis_parts:via_04_no_front_mask, F.Cu at (127.9, 102.6)
- added ?: , alis_parts:via_04_no_front_mask, F.Cu at (131.5, 104.1)
- added ?: , alis_parts:via_04_no_front_mask, F.Cu at (130.2, 104.4)
- added ?: , alis_parts:via_04_no_front_mask, F.Cu at (129.3, 103.7)
- added ?: , alis_parts:via_04_no_front_mask, F.Cu at (125.9, 104.9)
- added ?: , alis_parts:via_04_no_front_mask, F.Cu at (124.2, 110.6)
- added ?: , alis_parts:via_04_no_front_mask, F.Cu at (111.8, 113.0)
- added ?: , alis_parts:via_04_no_front_mask, F.Cu at (123.5, 111.0)
- added ?: , alis_parts:via_04_no_front_mask, F.Cu at (125.7, 110.6)
- added ?: , alis_parts:via_04_no_front_mask, F.Cu at (125.0, 110.6)
- added ?: , alis_parts:via_04_no_front_mask, F.Cu at (126.5, 110.6)
- added ?: , alis_parts:via_04_no_front_mask, F.Cu at (129.9, 96.2)
- added ?: , alis_parts:via_04_no_front_mask, F.Cu at (129.9, 95.5)
- added ?: , alis_parts:via_04_no_front_mask, F.Cu at (131.4, 95.5)
- added ?: , alis_parts:via_04_no_front_mask, F.Cu at (130.6, 95.5)
- added ?: , alis_parts:via_04_no_front_mask, F.Cu at (129.1, 95.5)
- added ?: , alis_parts:via_04_no_front_mask, F.Cu at (127.9, 93.1)
- added ?: , alis_parts:via_04_no_front_mask, F.Cu at (113.3, 113.0)
- added ?: , alis_parts:via_04_no_front_mask, F.Cu at (126.4, 93.1)
- added ?: , alis_parts:via_04_no_front_mask, F.Cu at (125.7, 93.1)
- added ?: , alis_parts:via_04_no_front_mask, F.Cu at (124.9, 93.1)
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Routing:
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- removed copper zone on B.Cu, net VBAT
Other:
- copper layers 4 -> 2
- board text added: "Monkeybrain v0.1 © Alexander Tuxen 2016"

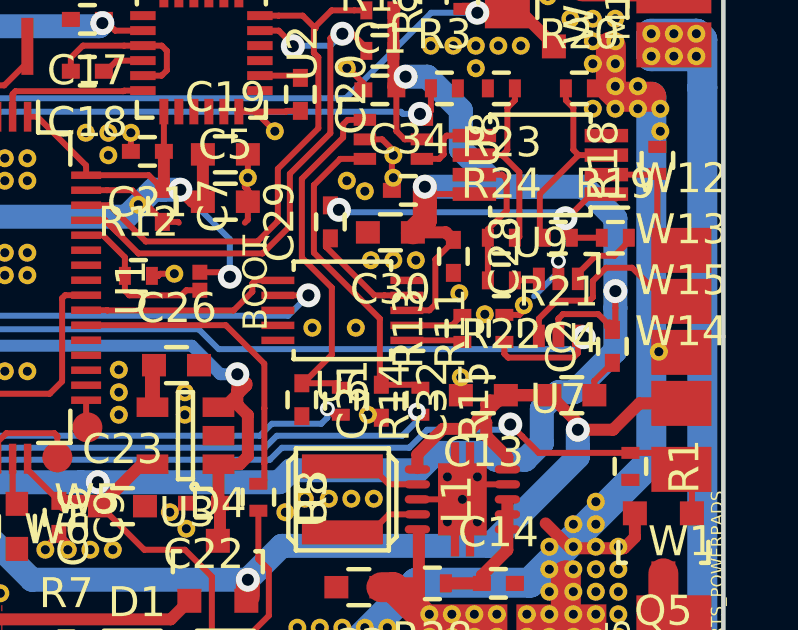
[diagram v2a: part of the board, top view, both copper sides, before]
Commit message: fixing switch polarity
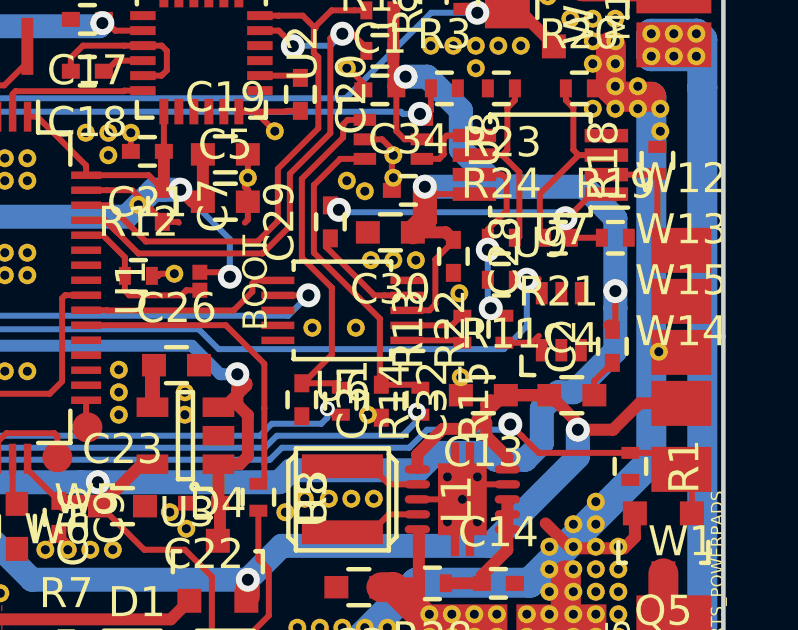
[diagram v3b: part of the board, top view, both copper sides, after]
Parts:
- removed the ? at (131.5, 104.1)
- removed the ? at (130.2, 104.4)
- M1, M2, M3: value (none) -> ALIS-CUSTOM-PARTS_POWERPADS
- moved R22 1.63 mm to (130.8, 104.9), turned to 90 degrees
- moved R11 1.62 mm to (130.7, 103.3), turned to 180 degrees
- moved U7 0.49 mm to (132.7, 104.7), turned to 0 degrees
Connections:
- U7 pad 1: Net-(R19-Pad2) -> Net-(R22-Pad1)
- U7 pad 3: Net-(R22-Pad1) -> Net-(R19-Pad2)
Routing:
- net VIDEO_OUT: track 6.81 -> 0.00 mm
- net BW_MASK: track 34.5 -> 30.8 mm
- net GND: track 132.8 -> 129.9 mm, vias 1 -> 0
- net 3.3V: track 157.5 -> 154.8 mm
- net Net-(R19-Pad2): track 2.32 -> 0.00 mm
- net bw_buffered: track 4.87 -> 6.52 mm, vias 0 -> 2
- net VIDEO_IN: track 4.91 -> 3.90 mm
